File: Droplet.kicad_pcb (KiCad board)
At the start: 2 copper layers, 34.6 x 16.4 mm, 34 parts, among them J1 Conn_01x05, J10 Conn_01x01, J11 Conn_01x01, J12 Conn_01x01, J2 Conn_01x05, J3 Conn_01x01, J4 Conn_01x01, J5 Conn_01x01, J6 Conn_01x01, J7 Conn_01x01, J8 Conn_01x01, J9 Conn_01x01, U1 ATtiny202-SS, U2 IRM-H638T/TR2

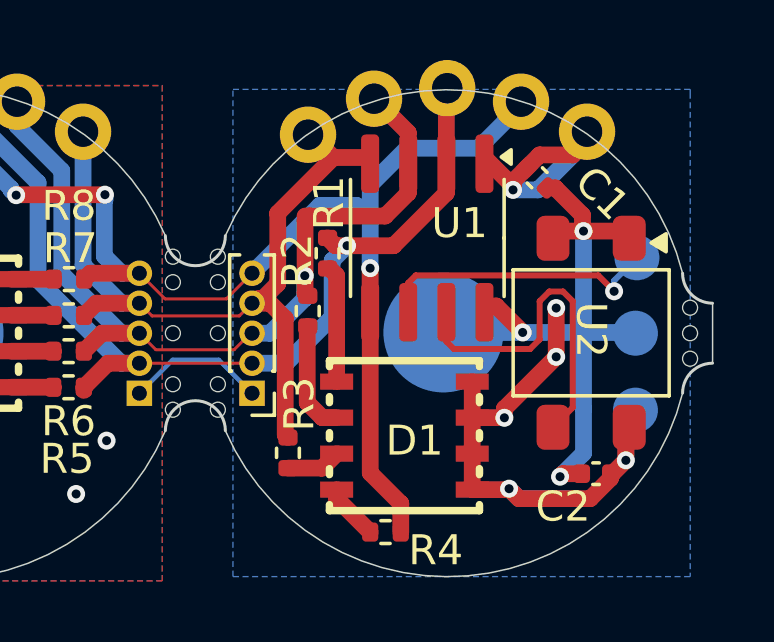
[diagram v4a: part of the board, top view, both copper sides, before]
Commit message: add larger battery terminal
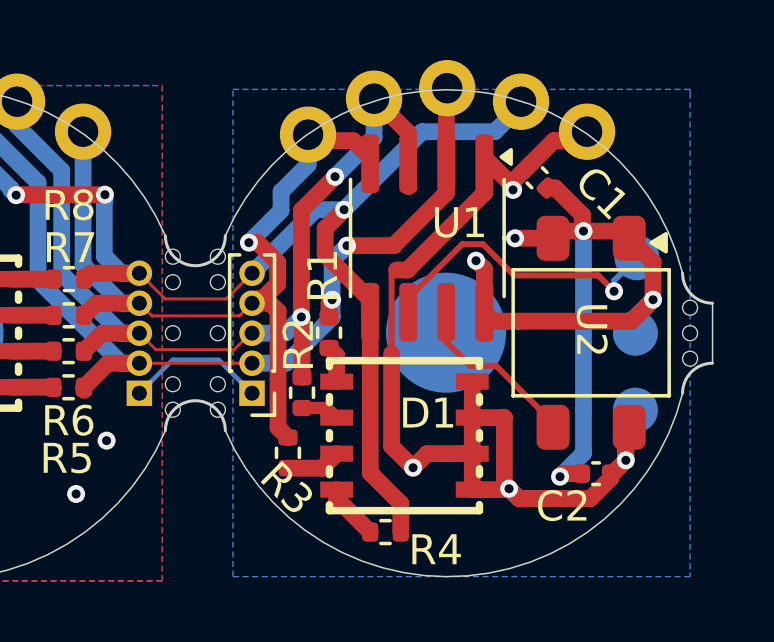
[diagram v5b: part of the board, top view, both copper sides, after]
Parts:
- moved R2 2.73 mm to (113.5, 36.4)
- moved R1 2.65 mm to (114.4, 34.4)
- moved TP2 0.09 mm to (118.3, 34.4)
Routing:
- net VBATT: track 35.1 -> 45.2 mm, vias 16 -> 14
- net GND: track 22.2 -> 28.6 mm, vias 3 -> 5
- net /PA3: track 11.4 -> 5.81 mm
- net Net-(D1-Pad2): track 3.94 -> 1.29 mm
- net Net-(D1-Pad4): track 3.74 -> 1.29 mm
- net /PA7: track 30.6 -> 32.4 mm, vias 1 -> 2
- net /PA1: track 27.5 -> 29.3 mm, vias 0 -> 1
- net /PA0: track 10.6 -> 11.1 mm
- net /PA6: track 33.2 -> 33.1 mm, vias 1 -> 2

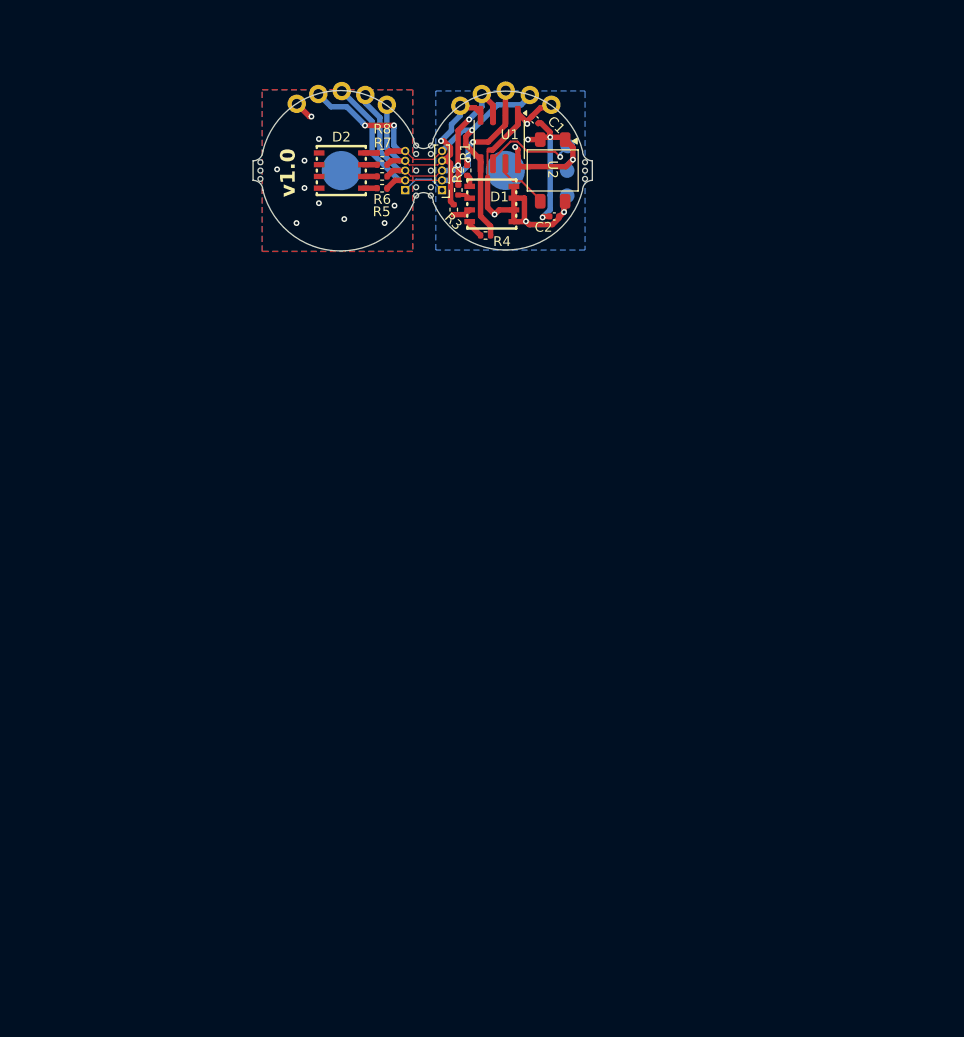
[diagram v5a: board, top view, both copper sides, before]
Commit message: 10 LED pair panel
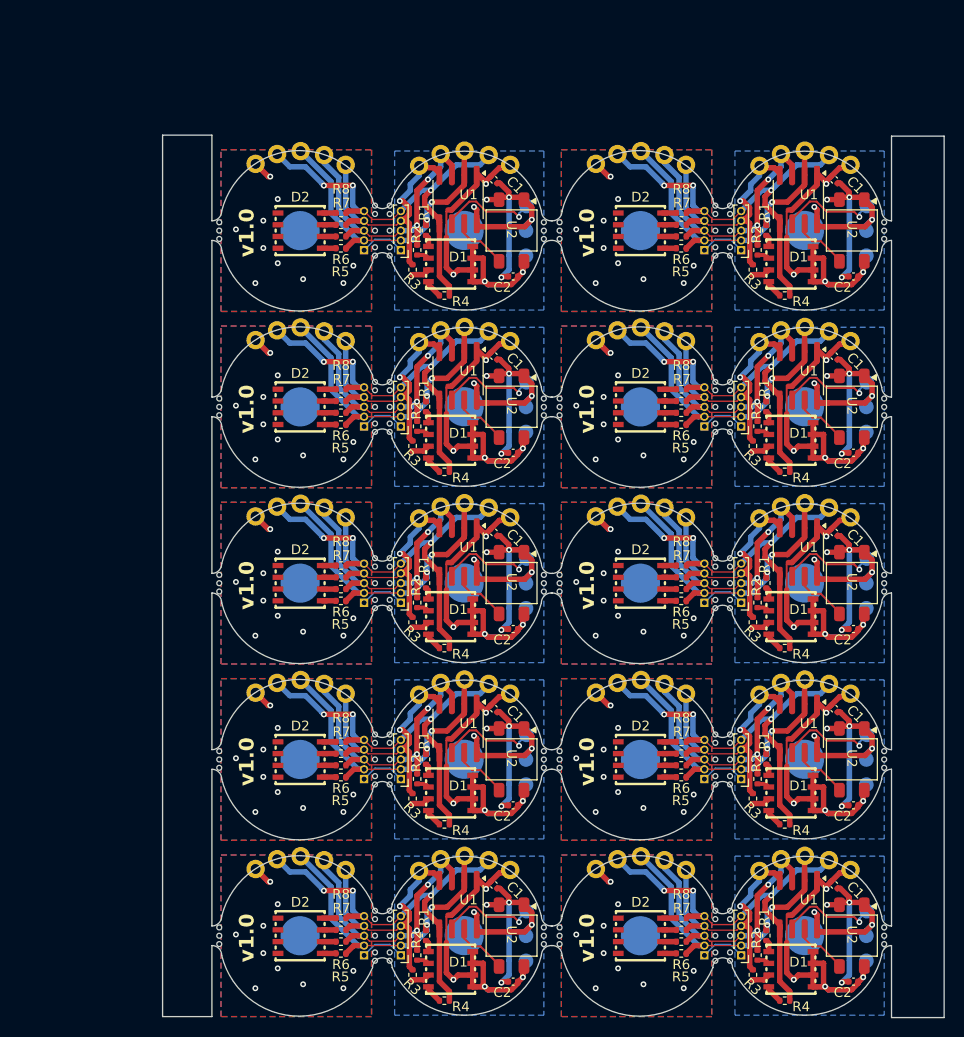
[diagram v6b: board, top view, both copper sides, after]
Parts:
- added C1: 100nF, Capacitor_SMD:C_0402_1005Metric, F.Cu at (117.1, 53.4)
- added C1: 100nF, Capacitor_SMD:C_0402_1005Metric, F.Cu at (151.9, 35.4)
- added C1: 100nF, Capacitor_SMD:C_0402_1005Metric, F.Cu at (151.9, 71.4)
- added C1: 100nF, Capacitor_SMD:C_0402_1005Metric, F.Cu at (117.1, 89.4)
- added C1: 100nF, Capacitor_SMD:C_0402_1005Metric, F.Cu at (151.9, 53.4)
- added C1: 100nF, Capacitor_SMD:C_0402_1005Metric, F.Cu at (117.1, 107.4)
- added C1: 100nF, Capacitor_SMD:C_0402_1005Metric, F.Cu at (117.1, 71.4)
- added C1: 100nF, Capacitor_SMD:C_0402_1005Metric, F.Cu at (117.1, 35.4)
- added C1: 100nF, Capacitor_SMD:C_0402_1005Metric, F.Cu at (151.9, 89.4)
- added C2: 100nF, Capacitor_SMD:C_0402_1005Metric, F.Cu at (119.1, 117.2)
- added C2: 100nF, Capacitor_SMD:C_0402_1005Metric, F.Cu at (119.1, 63.2)
- added C2: 100nF, Capacitor_SMD:C_0402_1005Metric, F.Cu at (119.1, 99.2)
- added C2: 100nF, Capacitor_SMD:C_0402_1005Metric, F.Cu at (153.8, 45.2)
- added C2: 100nF, Capacitor_SMD:C_0402_1005Metric, F.Cu at (153.8, 63.2)
- added C2: 100nF, Capacitor_SMD:C_0402_1005Metric, F.Cu at (119.1, 81.2)
- added C2: 100nF, Capacitor_SMD:C_0402_1005Metric, F.Cu at (153.8, 99.2)
- added C2: 100nF, Capacitor_SMD:C_0402_1005Metric, F.Cu at (153.8, 81.2)
- added C2: 100nF, Capacitor_SMD:C_0402_1005Metric, F.Cu at (119.1, 45.2)
- added D1: HL-5050RGBW-S1-A27, easyeda2kicad:LED-SMD_8P-L5.0-W5.0-P1.20_HL-5050RGBW-S1-A27, F.Cu at (147.5, 80.0)
- added D1: HL-5050RGBW-S1-A27, easyeda2kicad:LED-SMD_8P-L5.0-W5.0-P1.20_HL-5050RGBW-S1-A27, F.Cu at (112.7, 62.0)
- added D1: HL-5050RGBW-S1-A27, easyeda2kicad:LED-SMD_8P-L5.0-W5.0-P1.20_HL-5050RGBW-S1-A27, F.Cu at (112.7, 98.0)
- added D1: HL-5050RGBW-S1-A27, easyeda2kicad:LED-SMD_8P-L5.0-W5.0-P1.20_HL-5050RGBW-S1-A27, F.Cu at (147.5, 62.0)
- added D1: HL-5050RGBW-S1-A27, easyeda2kicad:LED-SMD_8P-L5.0-W5.0-P1.20_HL-5050RGBW-S1-A27, F.Cu at (147.5, 44.0)
- added D1: HL-5050RGBW-S1-A27, easyeda2kicad:LED-SMD_8P-L5.0-W5.0-P1.20_HL-5050RGBW-S1-A27, F.Cu at (112.7, 116.0)
- added D1: HL-5050RGBW-S1-A27, easyeda2kicad:LED-SMD_8P-L5.0-W5.0-P1.20_HL-5050RGBW-S1-A27, F.Cu at (112.7, 44.0)
- added D1: HL-5050RGBW-S1-A27, easyeda2kicad:LED-SMD_8P-L5.0-W5.0-P1.20_HL-5050RGBW-S1-A27, F.Cu at (147.5, 98.0)
- added D1: HL-5050RGBW-S1-A27, easyeda2kicad:LED-SMD_8P-L5.0-W5.0-P1.20_HL-5050RGBW-S1-A27, F.Cu at (112.7, 80.0)
- added D2: HL-5050RGBW-S1-A27, easyeda2kicad:LED-SMD_8P-L5.0-W5.0-P1.20_HL-5050RGBW-S1-A27, F.Cu at (97.3, 40.5)
- added D2: HL-5050RGBW-S1-A27, easyeda2kicad:LED-SMD_8P-L5.0-W5.0-P1.20_HL-5050RGBW-S1-A27, F.Cu at (132.1, 40.5)
- added D2: HL-5050RGBW-S1-A27, easyeda2kicad:LED-SMD_8P-L5.0-W5.0-P1.20_HL-5050RGBW-S1-A27, F.Cu at (132.1, 58.5)
- added D2: HL-5050RGBW-S1-A27, easyeda2kicad:LED-SMD_8P-L5.0-W5.0-P1.20_HL-5050RGBW-S1-A27, F.Cu at (97.3, 94.5)
- added D2: HL-5050RGBW-S1-A27, easyeda2kicad:LED-SMD_8P-L5.0-W5.0-P1.20_HL-5050RGBW-S1-A27, F.Cu at (97.3, 112.5)
- added D2: HL-5050RGBW-S1-A27, easyeda2kicad:LED-SMD_8P-L5.0-W5.0-P1.20_HL-5050RGBW-S1-A27, F.Cu at (97.3, 58.5)
- added D2: HL-5050RGBW-S1-A27, easyeda2kicad:LED-SMD_8P-L5.0-W5.0-P1.20_HL-5050RGBW-S1-A27, F.Cu at (132.1, 94.5)
- added D2: HL-5050RGBW-S1-A27, easyeda2kicad:LED-SMD_8P-L5.0-W5.0-P1.20_HL-5050RGBW-S1-A27, F.Cu at (132.1, 76.5)
- added D2: HL-5050RGBW-S1-A27, easyeda2kicad:LED-SMD_8P-L5.0-W5.0-P1.20_HL-5050RGBW-S1-A27, F.Cu at (97.3, 76.5)
- added J1: Conn_01x05, Connector_PinHeader_1.00mm:PinHeader_1x05_P1.00mm_Vertical, B.Cu at (103.9, 78.5)
- added J1: Conn_01x05, Connector_PinHeader_1.00mm:PinHeader_1x05_P1.00mm_Vertical, B.Cu at (138.6, 78.5)
- added J1: Conn_01x05, Connector_PinHeader_1.00mm:PinHeader_1x05_P1.00mm_Vertical, B.Cu at (103.9, 96.5)
- added J1: Conn_01x05, Connector_PinHeader_1.00mm:PinHeader_1x05_P1.00mm_Vertical, B.Cu at (138.6, 42.5)
- added J1: Conn_01x05, Connector_PinHeader_1.00mm:PinHeader_1x05_P1.00mm_Vertical, B.Cu at (103.9, 60.5)
- added J1: Conn_01x05, Connector_PinHeader_1.00mm:PinHeader_1x05_P1.00mm_Vertical, B.Cu at (138.6, 60.5)
- added J1: Conn_01x05, Connector_PinHeader_1.00mm:PinHeader_1x05_P1.00mm_Vertical, B.Cu at (138.6, 96.5)
- added J1: Conn_01x05, Connector_PinHeader_1.00mm:PinHeader_1x05_P1.00mm_Vertical, B.Cu at (103.9, 114.5)
- added J1: Conn_01x05, Connector_PinHeader_1.00mm:PinHeader_1x05_P1.00mm_Vertical, B.Cu at (103.9, 42.5)
- added J10: Conn_01x01, Custom:1x01_P2.54mm castellated, F.Cu at (134.5, 50.8)
- added J10: Conn_01x01, Custom:1x01_P2.54mm castellated, F.Cu at (99.8, 86.8)
- added J10: Conn_01x01, Custom:1x01_P2.54mm castellated, F.Cu at (99.8, 104.8)
- added J10: Conn_01x01, Custom:1x01_P2.54mm castellated, F.Cu at (134.5, 32.8)
- added J10: Conn_01x01, Custom:1x01_P2.54mm castellated, F.Cu at (134.5, 68.8)
- added J10: Conn_01x01, Custom:1x01_P2.54mm castellated, F.Cu at (99.8, 32.8)
- added J10: Conn_01x01, Custom:1x01_P2.54mm castellated, F.Cu at (99.8, 50.8)
- added J10: Conn_01x01, Custom:1x01_P2.54mm castellated, F.Cu at (99.8, 68.8)
- added J10: Conn_01x01, Custom:1x01_P2.54mm castellated, F.Cu at (134.5, 86.8)
- added J11: Conn_01x01, Custom:1x01_P2.54mm castellated, F.Cu at (97.4, 68.4)
- added J11: Conn_01x01, Custom:1x01_P2.54mm castellated, F.Cu at (97.4, 32.4)
- added J11: Conn_01x01, Custom:1x01_P2.54mm castellated, F.Cu at (97.4, 104.4)
- added J11: Conn_01x01, Custom:1x01_P2.54mm castellated, F.Cu at (132.1, 68.4)
- added J11: Conn_01x01, Custom:1x01_P2.54mm castellated, F.Cu at (97.4, 50.4)
- added J11: Conn_01x01, Custom:1x01_P2.54mm castellated, F.Cu at (97.4, 86.4)
- added J11: Conn_01x01, Custom:1x01_P2.54mm castellated, F.Cu at (132.1, 50.4)
- added J11: Conn_01x01, Custom:1x01_P2.54mm castellated, F.Cu at (132.1, 86.4)
- added J11: Conn_01x01, Custom:1x01_P2.54mm castellated, F.Cu at (132.1, 32.4)
- added J12: Conn_01x01, Custom:1x01_P2.54mm castellated, F.Cu at (92.8, 105.7)
- added J12: Conn_01x01, Custom:1x01_P2.54mm castellated, F.Cu at (92.8, 51.7)
- added J12: Conn_01x01, Custom:1x01_P2.54mm castellated, F.Cu at (92.8, 87.7)
- added J12: Conn_01x01, Custom:1x01_P2.54mm castellated, F.Cu at (127.5, 51.7)
- added J12: Conn_01x01, Custom:1x01_P2.54mm castellated, F.Cu at (127.5, 87.7)
- added J12: Conn_01x01, Custom:1x01_P2.54mm castellated, F.Cu at (92.8, 69.7)
- added J12: Conn_01x01, Custom:1x01_P2.54mm castellated, F.Cu at (127.5, 69.7)
- added J12: Conn_01x01, Custom:1x01_P2.54mm castellated, F.Cu at (92.8, 33.7)
- added J12: Conn_01x01, Custom:1x01_P2.54mm castellated, F.Cu at (127.5, 33.7)
- added J2: Conn_01x05, Connector_PinHeader_1.00mm:PinHeader_1x05_P1.00mm_Vertical, F.Cu at (142.4, 78.5)
- added J2: Conn_01x05, Connector_PinHeader_1.00mm:PinHeader_1x05_P1.00mm_Vertical, F.Cu at (107.6, 42.5)
- added J2: Conn_01x05, Connector_PinHeader_1.00mm:PinHeader_1x05_P1.00mm_Vertical, F.Cu at (107.6, 78.5)
- added J2: Conn_01x05, Connector_PinHeader_1.00mm:PinHeader_1x05_P1.00mm_Vertical, F.Cu at (142.4, 60.5)
- added J2: Conn_01x05, Connector_PinHeader_1.00mm:PinHeader_1x05_P1.00mm_Vertical, F.Cu at (107.6, 96.5)
- added J2: Conn_01x05, Connector_PinHeader_1.00mm:PinHeader_1x05_P1.00mm_Vertical, F.Cu at (142.4, 42.5)
- added J2: Conn_01x05, Connector_PinHeader_1.00mm:PinHeader_1x05_P1.00mm_Vertical, F.Cu at (142.4, 96.5)
- added J2: Conn_01x05, Connector_PinHeader_1.00mm:PinHeader_1x05_P1.00mm_Vertical, F.Cu at (107.6, 60.5)
- added J2: Conn_01x05, Connector_PinHeader_1.00mm:PinHeader_1x05_P1.00mm_Vertical, F.Cu at (107.6, 114.5)
- added J3: Conn_01x01, Custom:1x01_P2.54mm castellated, F.Cu at (114.1, 86.4)
- added J3: Conn_01x01, Custom:1x01_P2.54mm castellated, F.Cu at (114.1, 68.4)
- added J3: Conn_01x01, Custom:1x01_P2.54mm castellated, F.Cu at (148.9, 86.4)
- added J3: Conn_01x01, Custom:1x01_P2.54mm castellated, F.Cu at (148.9, 32.4)
- added J3: Conn_01x01, Custom:1x01_P2.54mm castellated, F.Cu at (114.1, 50.4)
- added J3: Conn_01x01, Custom:1x01_P2.54mm castellated, F.Cu at (114.1, 32.4)
- added J3: Conn_01x01, Custom:1x01_P2.54mm castellated, F.Cu at (148.9, 50.4)
- added J3: Conn_01x01, Custom:1x01_P2.54mm castellated, F.Cu at (148.9, 68.4)
- added J3: Conn_01x01, Custom:1x01_P2.54mm castellated, F.Cu at (114.1, 104.4)
- added J4: Conn_01x01, Custom:1x01_P2.54mm castellated, F.Cu at (146.4, 50.7)
- added J4: Conn_01x01, Custom:1x01_P2.54mm castellated, F.Cu at (111.7, 86.7)
- added J4: Conn_01x01, Custom:1x01_P2.54mm castellated, F.Cu at (111.7, 50.7)
- added J4: Conn_01x01, Custom:1x01_P2.54mm castellated, F.Cu at (111.7, 68.7)
- added J4: Conn_01x01, Custom:1x01_P2.54mm castellated, F.Cu at (146.4, 68.7)
- added J4: Conn_01x01, Custom:1x01_P2.54mm castellated, F.Cu at (146.4, 86.7)
- added J4: Conn_01x01, Custom:1x01_P2.54mm castellated, F.Cu at (111.7, 104.7)
- added J4: Conn_01x01, Custom:1x01_P2.54mm castellated, F.Cu at (146.4, 32.7)
- added J4: Conn_01x01, Custom:1x01_P2.54mm castellated, F.Cu at (111.7, 32.7)
- added J5: Conn_01x01, Custom:1x01_P2.54mm castellated, F.Cu at (109.5, 87.9)
- added J5: Conn_01x01, Custom:1x01_P2.54mm castellated, F.Cu at (109.5, 33.9)
- added J5: Conn_01x01, Custom:1x01_P2.54mm castellated, F.Cu at (144.2, 51.9)
- added J5: Conn_01x01, Custom:1x01_P2.54mm castellated, F.Cu at (109.5, 105.9)
- added J5: Conn_01x01, Custom:1x01_P2.54mm castellated, F.Cu at (144.2, 69.9)
- added J5: Conn_01x01, Custom:1x01_P2.54mm castellated, F.Cu at (144.2, 87.9)
- added J5: Conn_01x01, Custom:1x01_P2.54mm castellated, F.Cu at (109.5, 51.9)
- added J5: Conn_01x01, Custom:1x01_P2.54mm castellated, F.Cu at (109.5, 69.9)
- added J5: Conn_01x01, Custom:1x01_P2.54mm castellated, F.Cu at (144.2, 33.9)
- added J6: Conn_01x01, Custom:1x01_P2.54mm castellated, F.Cu at (116.6, 32.8)
- added J6: Conn_01x01, Custom:1x01_P2.54mm castellated, F.Cu at (151.3, 32.8)
- added J6: Conn_01x01, Custom:1x01_P2.54mm castellated, F.Cu at (151.3, 86.8)
- added J6: Conn_01x01, Custom:1x01_P2.54mm castellated, F.Cu at (116.6, 68.8)
- added J6: Conn_01x01, Custom:1x01_P2.54mm castellated, F.Cu at (116.6, 86.8)
- added J6: Conn_01x01, Custom:1x01_P2.54mm castellated, F.Cu at (151.3, 50.8)
- added J6: Conn_01x01, Custom:1x01_P2.54mm castellated, F.Cu at (151.3, 68.8)
- added J6: Conn_01x01, Custom:1x01_P2.54mm castellated, F.Cu at (116.6, 50.8)
- added J6: Conn_01x01, Custom:1x01_P2.54mm castellated, F.Cu at (116.6, 104.8)
- added J7: Conn_01x01, Custom:1x01_P2.54mm castellated, F.Cu at (153.5, 33.8)
- added J7: Conn_01x01, Custom:1x01_P2.54mm castellated, F.Cu at (118.8, 87.8)
- added J7: Conn_01x01, Custom:1x01_P2.54mm castellated, F.Cu at (118.8, 51.8)
- added J7: Conn_01x01, Custom:1x01_P2.54mm castellated, F.Cu at (153.5, 69.8)
- added J7: Conn_01x01, Custom:1x01_P2.54mm castellated, F.Cu at (118.8, 105.8)
- added J7: Conn_01x01, Custom:1x01_P2.54mm castellated, F.Cu at (118.8, 33.8)
- added J7: Conn_01x01, Custom:1x01_P2.54mm castellated, F.Cu at (153.5, 51.8)
- added J7: Conn_01x01, Custom:1x01_P2.54mm castellated, F.Cu at (118.8, 69.8)
- added J7: Conn_01x01, Custom:1x01_P2.54mm castellated, F.Cu at (153.5, 87.8)
- added J8: Conn_01x01, Custom:1x01_P2.54mm castellated, F.Cu at (95.0, 86.7)
- added J8: Conn_01x01, Custom:1x01_P2.54mm castellated, F.Cu at (129.7, 86.7)
- added J8: Conn_01x01, Custom:1x01_P2.54mm castellated, F.Cu at (129.7, 50.7)
- added J8: Conn_01x01, Custom:1x01_P2.54mm castellated, F.Cu at (129.7, 68.7)
- added J8: Conn_01x01, Custom:1x01_P2.54mm castellated, F.Cu at (95.0, 50.7)
- added J8: Conn_01x01, Custom:1x01_P2.54mm castellated, F.Cu at (95.0, 104.7)
- added J8: Conn_01x01, Custom:1x01_P2.54mm castellated, F.Cu at (95.0, 32.7)
- added J8: Conn_01x01, Custom:1x01_P2.54mm castellated, F.Cu at (95.0, 68.7)
- added J8: Conn_01x01, Custom:1x01_P2.54mm castellated, F.Cu at (129.7, 32.7)
- added J9: Conn_01x01, Custom:1x01_P2.54mm castellated, F.Cu at (102.0, 105.8)
- added J9: Conn_01x01, Custom:1x01_P2.54mm castellated, F.Cu at (136.7, 87.8)
- added J9: Conn_01x01, Custom:1x01_P2.54mm castellated, F.Cu at (102.0, 69.8)
- added J9: Conn_01x01, Custom:1x01_P2.54mm castellated, F.Cu at (136.7, 51.8)
- added J9: Conn_01x01, Custom:1x01_P2.54mm castellated, F.Cu at (102.0, 87.8)
- added J9: Conn_01x01, Custom:1x01_P2.54mm castellated, F.Cu at (136.7, 33.8)
- added J9: Conn_01x01, Custom:1x01_P2.54mm castellated, F.Cu at (102.0, 51.8)
- added J9: Conn_01x01, Custom:1x01_P2.54mm castellated, F.Cu at (136.7, 69.8)
- added J9: Conn_01x01, Custom:1x01_P2.54mm castellated, F.Cu at (102.0, 33.8)
- added R1: 27, Resistor_SMD:R_0402_1005Metric, F.Cu at (110.2, 58.5)
- added R1: 27, Resistor_SMD:R_0402_1005Metric, F.Cu at (144.9, 76.5)
- added R1: 27, Resistor_SMD:R_0402_1005Metric, F.Cu at (110.2, 40.5)
- added R1: 27, Resistor_SMD:R_0402_1005Metric, F.Cu at (144.9, 94.5)
- added R1: 27, Resistor_SMD:R_0402_1005Metric, F.Cu at (110.2, 94.5)
- added R1: 27, Resistor_SMD:R_0402_1005Metric, F.Cu at (110.2, 112.5)
- added R1: 27, Resistor_SMD:R_0402_1005Metric, F.Cu at (144.9, 58.5)
- added R1: 27, Resistor_SMD:R_0402_1005Metric, F.Cu at (110.2, 76.5)
- added R1: 27, Resistor_SMD:R_0402_1005Metric, F.Cu at (144.9, 40.5)
- added R2: 27, Resistor_SMD:R_0402_1005Metric, F.Cu at (144.0, 78.5)
- added R2: 27, Resistor_SMD:R_0402_1005Metric, F.Cu at (109.3, 60.5)
- added R2: 27, Resistor_SMD:R_0402_1005Metric, F.Cu at (109.3, 96.5)
- added R2: 27, Resistor_SMD:R_0402_1005Metric, F.Cu at (109.3, 114.5)
- added R2: 27, Resistor_SMD:R_0402_1005Metric, F.Cu at (144.0, 96.5)
- added R2: 27, Resistor_SMD:R_0402_1005Metric, F.Cu at (144.0, 60.5)
- added R2: 27, Resistor_SMD:R_0402_1005Metric, F.Cu at (109.3, 78.5)
- added R2: 27, Resistor_SMD:R_0402_1005Metric, F.Cu at (144.0, 42.5)
- added R2: 27, Resistor_SMD:R_0402_1005Metric, F.Cu at (109.3, 42.5)
- added R3: 27, Resistor_SMD:R_0402_1005Metric, F.Cu at (108.8, 62.5)
- added R3: 27, Resistor_SMD:R_0402_1005Metric, F.Cu at (143.6, 44.5)
- added R3: 27, Resistor_SMD:R_0402_1005Metric, F.Cu at (108.8, 98.5)
- added R3: 27, Resistor_SMD:R_0402_1005Metric, F.Cu at (143.6, 62.5)
- added R3: 27, Resistor_SMD:R_0402_1005Metric, F.Cu at (108.8, 116.5)
- added R3: 27, Resistor_SMD:R_0402_1005Metric, F.Cu at (143.6, 98.5)
- added R3: 27, Resistor_SMD:R_0402_1005Metric, F.Cu at (143.6, 80.5)
- added R3: 27, Resistor_SMD:R_0402_1005Metric, F.Cu at (108.8, 80.5)
- added R3: 27, Resistor_SMD:R_0402_1005Metric, F.Cu at (108.8, 44.5)
- added R4: 75, Resistor_SMD:R_0402_1005Metric, F.Cu at (146.8, 101.2)
- added R4: 75, Resistor_SMD:R_0402_1005Metric, F.Cu at (112.1, 83.2)
- added R4: 75, Resistor_SMD:R_0402_1005Metric, F.Cu at (146.8, 83.2)
- added R4: 75, Resistor_SMD:R_0402_1005Metric, F.Cu at (112.1, 65.2)
- added R4: 75, Resistor_SMD:R_0402_1005Metric, F.Cu at (112.1, 47.2)
- added R4: 75, Resistor_SMD:R_0402_1005Metric, F.Cu at (112.1, 119.2)
- added R4: 75, Resistor_SMD:R_0402_1005Metric, F.Cu at (112.1, 101.2)
- added R4: 75, Resistor_SMD:R_0402_1005Metric, F.Cu at (146.8, 65.2)
- added R4: 75, Resistor_SMD:R_0402_1005Metric, F.Cu at (146.8, 47.2)
- added R5: 27, Resistor_SMD:R_0402_1005Metric, F.Cu at (101.5, 78.4)
- added R5: 27, Resistor_SMD:R_0402_1005Metric, F.Cu at (101.5, 60.4)
- added R5: 27, Resistor_SMD:R_0402_1005Metric, F.Cu at (136.3, 78.4)
- added R5: 27, Resistor_SMD:R_0402_1005Metric, F.Cu at (101.5, 96.4)
- added R5: 27, Resistor_SMD:R_0402_1005Metric, F.Cu at (136.3, 60.4)
- added R5: 27, Resistor_SMD:R_0402_1005Metric, F.Cu at (136.3, 42.4)
- added R5: 27, Resistor_SMD:R_0402_1005Metric, F.Cu at (101.5, 42.4)
- added R5: 27, Resistor_SMD:R_0402_1005Metric, F.Cu at (101.5, 114.4)
- added R5: 27, Resistor_SMD:R_0402_1005Metric, F.Cu at (136.3, 96.4)
- added R6: 27, Resistor_SMD:R_0402_1005Metric, F.Cu at (136.3, 77.1)
- added R6: 27, Resistor_SMD:R_0402_1005Metric, F.Cu at (136.3, 95.1)
- added R6: 27, Resistor_SMD:R_0402_1005Metric, F.Cu at (101.5, 113.1)
- added R6: 27, Resistor_SMD:R_0402_1005Metric, F.Cu at (101.5, 59.1)
- added R6: 27, Resistor_SMD:R_0402_1005Metric, F.Cu at (101.5, 41.1)
- added R6: 27, Resistor_SMD:R_0402_1005Metric, F.Cu at (136.3, 59.1)
- added R6: 27, Resistor_SMD:R_0402_1005Metric, F.Cu at (101.5, 77.1)
- added R6: 27, Resistor_SMD:R_0402_1005Metric, F.Cu at (101.5, 95.1)
- added R6: 27, Resistor_SMD:R_0402_1005Metric, F.Cu at (136.3, 41.1)
- added R7: 27, Resistor_SMD:R_0402_1005Metric, F.Cu at (136.3, 40.0)
- added R7: 27, Resistor_SMD:R_0402_1005Metric, F.Cu at (101.5, 112.0)
- added R7: 27, Resistor_SMD:R_0402_1005Metric, F.Cu at (101.5, 76.0)
- added R7: 27, Resistor_SMD:R_0402_1005Metric, F.Cu at (101.5, 94.0)
- added R7: 27, Resistor_SMD:R_0402_1005Metric, F.Cu at (101.5, 40.0)
- added R7: 27, Resistor_SMD:R_0402_1005Metric, F.Cu at (136.3, 94.0)
- added R7: 27, Resistor_SMD:R_0402_1005Metric, F.Cu at (136.3, 76.0)
- added R7: 27, Resistor_SMD:R_0402_1005Metric, F.Cu at (101.5, 58.0)
- added R7: 27, Resistor_SMD:R_0402_1005Metric, F.Cu at (136.3, 58.0)
- added R8: 75, Resistor_SMD:R_0402_1005Metric, F.Cu at (101.5, 74.7)
- added R8: 75, Resistor_SMD:R_0402_1005Metric, F.Cu at (101.5, 56.7)
- added R8: 75, Resistor_SMD:R_0402_1005Metric, F.Cu at (136.3, 38.7)
- added R8: 75, Resistor_SMD:R_0402_1005Metric, F.Cu at (101.5, 38.7)
- added R8: 75, Resistor_SMD:R_0402_1005Metric, F.Cu at (136.3, 92.7)
- added R8: 75, Resistor_SMD:R_0402_1005Metric, F.Cu at (136.3, 74.7)
- added R8: 75, Resistor_SMD:R_0402_1005Metric, F.Cu at (101.5, 92.7)
- added R8: 75, Resistor_SMD:R_0402_1005Metric, F.Cu at (136.3, 56.7)
- added R8: 75, Resistor_SMD:R_0402_1005Metric, F.Cu at (101.5, 110.7)
- added REF**: MouseBite-Slot_2.0x4.5mm_outset_D0.5mm_P0.85mm_5h_Trace, Panelization:MouseBite-Slot_2.0x4.5mm_outset_D0.5mm_P0.85mm_5h_Trace, F.Cu at (106.7, 76.5)
- added REF**: MouseBite-Part_2.0x2.0mm_outset_D0.5mm_P0.85mm_3h, Panelization:MouseBite-Part_2.0x2.0mm_outset_D0.5mm_P0.85mm_3h, F.Cu at (124.1, 58.5)
- added REF**: MouseBite-Slot_2.0x4.5mm_outset_D0.5mm_P0.85mm_5h_Trace, Panelization:MouseBite-Slot_2.0x4.5mm_outset_D0.5mm_P0.85mm_5h_Trace, F.Cu at (141.5, 58.5)
- added REF**: MouseBite-Slot_2.0x4.5mm_outset_D0.5mm_P0.85mm_5h_Trace, Panelization:MouseBite-Slot_2.0x4.5mm_outset_D0.5mm_P0.85mm_5h_Trace, F.Cu at (141.5, 76.5)
- added REF**: MouseBite-Part_2.0x2.0mm_outset_D0.5mm_P0.85mm_3h, Panelization:MouseBite-Part_2.0x2.0mm_outset_D0.5mm_P0.85mm_3h, F.Cu at (156.7, 94.5)
- added REF**: MouseBite-Part_2.0x2.0mm_outset_D0.5mm_P0.85mm_3h, Panelization:MouseBite-Part_2.0x2.0mm_outset_D0.5mm_P0.85mm_3h, F.Cu at (122.0, 58.5)
- added REF**: MouseBite-Part_2.0x2.0mm_outset_D0.5mm_P0.85mm_3h, Panelization:MouseBite-Part_2.0x2.0mm_outset_D0.5mm_P0.85mm_3h, F.Cu at (122.0, 40.5)
- added REF**: MouseBite-Part_2.0x2.0mm_outset_D0.5mm_P0.85mm_3h, Panelization:MouseBite-Part_2.0x2.0mm_outset_D0.5mm_P0.85mm_3h, F.Cu at (89.3, 58.5)
- added REF**: MouseBite-Part_2.0x2.0mm_outset_D0.5mm_P0.85mm_3h, Panelization:MouseBite-Part_2.0x2.0mm_outset_D0.5mm_P0.85mm_3h, F.Cu at (89.3, 94.5)
- added REF**: MouseBite-Part_2.0x2.0mm_outset_D0.5mm_P0.85mm_3h, Panelization:MouseBite-Part_2.0x2.0mm_outset_D0.5mm_P0.85mm_3h, F.Cu at (124.1, 76.5)
- added REF**: MouseBite-Part_2.0x2.0mm_outset_D0.5mm_P0.85mm_3h, Panelization:MouseBite-Part_2.0x2.0mm_outset_D0.5mm_P0.85mm_3h, F.Cu at (124.1, 40.5)
- added REF**: MouseBite-Part_2.0x2.0mm_outset_D0.5mm_P0.85mm_3h, Panelization:MouseBite-Part_2.0x2.0mm_outset_D0.5mm_P0.85mm_3h, F.Cu at (89.3, 40.5)
- added REF**: MouseBite-Part_2.0x2.0mm_outset_D0.5mm_P0.85mm_3h, Panelization:MouseBite-Part_2.0x2.0mm_outset_D0.5mm_P0.85mm_3h, F.Cu at (156.7, 76.5)
- added REF**: MouseBite-Part_2.0x2.0mm_outset_D0.5mm_P0.85mm_3h, Panelization:MouseBite-Part_2.0x2.0mm_outset_D0.5mm_P0.85mm_3h, F.Cu at (124.1, 94.5)
- added REF**: MouseBite-Part_2.0x2.0mm_outset_D0.5mm_P0.85mm_3h, Panelization:MouseBite-Part_2.0x2.0mm_outset_D0.5mm_P0.85mm_3h, F.Cu at (122.0, 76.5)
- added REF**: MouseBite-Slot_2.0x4.5mm_outset_D0.5mm_P0.85mm_5h_Trace, Panelization:MouseBite-Slot_2.0x4.5mm_outset_D0.5mm_P0.85mm_5h_Trace, F.Cu at (106.7, 94.5)
- added REF**: MouseBite-Slot_2.0x4.5mm_outset_D0.5mm_P0.85mm_5h_Trace, Panelization:MouseBite-Slot_2.0x4.5mm_outset_D0.5mm_P0.85mm_5h_Trace, F.Cu at (141.5, 40.5)
- added REF**: MouseBite-Part_2.0x2.0mm_outset_D0.5mm_P0.85mm_3h, Panelization:MouseBite-Part_2.0x2.0mm_outset_D0.5mm_P0.85mm_3h, F.Cu at (122.0, 112.5)
- added REF**: MouseBite-Slot_2.0x4.5mm_outset_D0.5mm_P0.85mm_5h_Trace, Panelization:MouseBite-Slot_2.0x4.5mm_outset_D0.5mm_P0.85mm_5h_Trace, F.Cu at (141.5, 94.5)
- added REF**: MouseBite-Part_2.0x2.0mm_outset_D0.5mm_P0.85mm_3h, Panelization:MouseBite-Part_2.0x2.0mm_outset_D0.5mm_P0.85mm_3h, F.Cu at (122.0, 94.5)
- added REF**: MouseBite-Part_2.0x2.0mm_outset_D0.5mm_P0.85mm_3h, Panelization:MouseBite-Part_2.0x2.0mm_outset_D0.5mm_P0.85mm_3h, F.Cu at (89.3, 112.5)
- added REF**: MouseBite-Slot_2.0x4.5mm_outset_D0.5mm_P0.85mm_5h_Trace, Panelization:MouseBite-Slot_2.0x4.5mm_outset_D0.5mm_P0.85mm_5h_Trace, F.Cu at (106.7, 58.5)
- added REF**: MouseBite-Slot_2.0x4.5mm_outset_D0.5mm_P0.85mm_5h_Trace, Panelization:MouseBite-Slot_2.0x4.5mm_outset_D0.5mm_P0.85mm_5h_Trace, F.Cu at (106.7, 112.5)
- added REF**: MouseBite-Slot_2.0x4.5mm_outset_D0.5mm_P0.85mm_5h_Trace, Panelization:MouseBite-Slot_2.0x4.5mm_outset_D0.5mm_P0.85mm_5h_Trace, F.Cu at (106.7, 40.5)
- added REF**: MouseBite-Part_2.0x2.0mm_outset_D0.5mm_P0.85mm_3h, Panelization:MouseBite-Part_2.0x2.0mm_outset_D0.5mm_P0.85mm_3h, F.Cu at (156.7, 40.5)
- added REF**: MouseBite-Part_2.0x2.0mm_outset_D0.5mm_P0.85mm_3h, Panelization:MouseBite-Part_2.0x2.0mm_outset_D0.5mm_P0.85mm_3h, F.Cu at (89.3, 76.5)
- added REF**: MouseBite-Part_2.0x2.0mm_outset_D0.5mm_P0.85mm_3h, Panelization:MouseBite-Part_2.0x2.0mm_outset_D0.5mm_P0.85mm_3h, F.Cu at (156.7, 58.5)
- added TP1: +, TestPoint:TestPoint_Pad_D4.0mm, B.Cu at (97.3, 112.5)
- added TP1: +, TestPoint:TestPoint_Pad_D4.0mm, B.Cu at (97.3, 58.5)
- added TP1: +, TestPoint:TestPoint_Pad_D4.0mm, B.Cu at (97.3, 94.5)
- added TP1: +, TestPoint:TestPoint_Pad_D4.0mm, B.Cu at (132.1, 40.5)
- added TP1: +, TestPoint:TestPoint_Pad_D4.0mm, B.Cu at (97.3, 76.5)
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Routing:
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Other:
- board size 34.6 x 16.4 mm -> 79.8 x 90.1 mm
- board text added: "CNC"

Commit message: major changes - add boost and mosfets
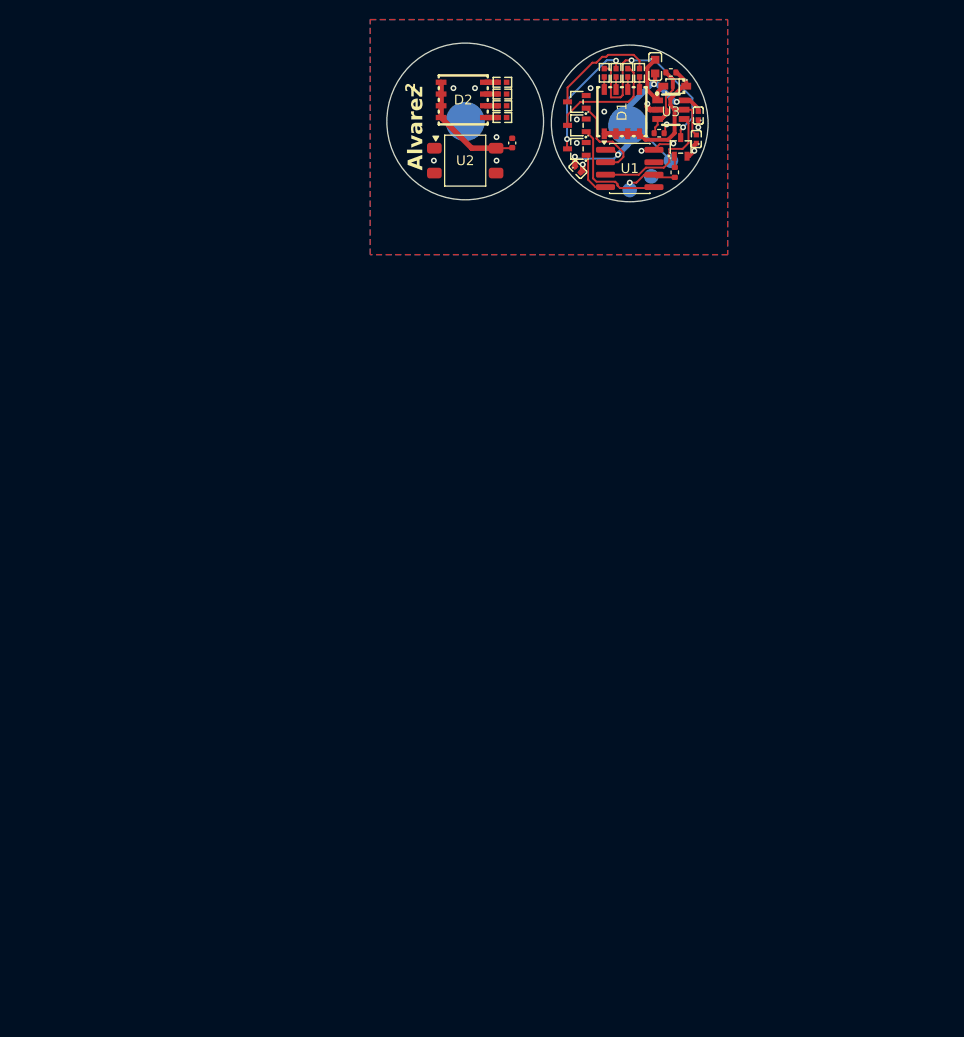
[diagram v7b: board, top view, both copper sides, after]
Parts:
- removed C1 (x10): 100nF, Capacitor_SMD:C_0402_1005Metric
- removed the C2 at (119.1, 117.2)
- removed the C2 at (153.8, 117.2)
- removed the C2 at (119.1, 63.2)
- removed the C2 at (119.1, 99.2)
- removed the C2 at (153.8, 45.2)
- removed the C2 at (153.8, 63.2)
- removed the C2 at (119.1, 81.2)
- removed the C2 at (153.8, 99.2)
- removed the C2 at (153.8, 81.2)
- removed the C2 at (119.1, 45.2)
- removed the D1 at (147.5, 80.0)
- removed the D1 at (112.7, 62.0)
- removed the D1 at (112.7, 98.0)
- removed the D1 at (147.5, 62.0)
- removed the D1 at (147.5, 44.0)
- removed the D1 at (147.5, 116.0)
- removed the D1 at (112.7, 116.0)
- removed the D1 at (112.7, 44.0)
- removed the D1 at (147.5, 98.0)
- removed the D1 at (112.7, 80.0)
- removed the D2 at (97.3, 40.5)
- removed the D2 at (132.1, 112.5)
- removed the D2 at (132.1, 40.5)
- removed the D2 at (132.1, 58.5)
- removed the D2 at (97.3, 94.5)
- removed the D2 at (97.3, 112.5)
- removed the D2 at (97.3, 58.5)
- removed the D2 at (132.1, 94.5)
- removed the D2 at (132.1, 76.5)
- removed the D2 at (97.3, 76.5)
- removed J1 (x10), J2 (x10): Conn_01x05, Connector_PinHeader_1.00mm:PinHeader_1x05_P1.00mm_Vertical
- removed J10 (x10), J11 (x10), J12 (x10), J3 (x10), J4 (x10), J5 (x10), J6 (x10), J7 (x10), J8 (x10), J9 (x10): Conn_01x01, Custom:1x01_P2.54mm castellated
- removed the R1 at (110.2, 58.5)
- removed the R1 at (144.9, 76.5)
- removed the R1 at (110.2, 40.5)
- removed the R1 at (144.9, 94.5)
- removed the R1 at (110.2, 94.5)
- removed the R1 at (110.2, 112.5)
- removed the R1 at (144.9, 58.5)
- removed the R1 at (110.2, 76.5)
- removed the R1 at (144.9, 40.5)
- removed the R1 at (144.9, 112.5)
- removed the R2 at (144.0, 78.5)
- removed the R2 at (109.3, 60.5)
- removed the R2 at (109.3, 96.5)
- removed the R2 at (109.3, 114.5)
- removed the R2 at (144.0, 96.5)
- removed the R2 at (144.0, 60.5)
- removed the R2 at (109.3, 78.5)
- removed the R2 at (144.0, 114.5)
- removed the R2 at (144.0, 42.5)
- removed the R2 at (109.3, 42.5)
- removed the R3 at (108.8, 62.5)
- removed the R3 at (143.6, 44.5)
- removed the R3 at (108.8, 98.5)
- removed the R3 at (143.6, 62.5)
- removed the R3 at (108.8, 116.5)
- removed the R3 at (143.6, 98.5)
- removed the R3 at (143.6, 80.5)
- removed the R3 at (108.8, 80.5)
- removed the R3 at (143.6, 116.5)
- removed the R3 at (108.8, 44.5)
- removed the R4 at (146.8, 101.2)
- removed the R4 at (146.8, 119.2)
- removed the R4 at (112.1, 83.2)
- removed the R4 at (146.8, 83.2)
- removed the R4 at (112.1, 65.2)
- removed the R4 at (112.1, 47.2)
- removed the R4 at (112.1, 119.2)
- removed the R4 at (112.1, 101.2)
- removed the R4 at (146.8, 65.2)
- removed the R4 at (146.8, 47.2)
- removed the R5 at (101.5, 78.4)
- removed the R5 at (101.5, 60.4)
- removed the R5 at (136.3, 78.4)
- removed the R5 at (101.5, 96.4)
- removed the R5 at (136.3, 60.4)
- removed the R5 at (136.3, 42.4)
- removed the R5 at (136.3, 114.4)
- removed the R5 at (101.5, 42.4)
- removed the R5 at (101.5, 114.4)
- removed the R5 at (136.3, 96.4)
- removed the R6 at (136.3, 77.1)
- removed the R6 at (136.3, 95.1)
- removed the R6 at (101.5, 113.1)
- removed the R6 at (101.5, 59.1)
- removed the R6 at (101.5, 41.1)
- removed the R6 at (136.3, 59.1)
- removed the R6 at (136.3, 113.1)
- removed the R6 at (101.5, 77.1)
- removed the R6 at (101.5, 95.1)
- removed the R6 at (136.3, 41.1)
- removed the R7 at (136.3, 40.0)
- removed the R7 at (101.5, 112.0)
- removed the R7 at (136.3, 112.0)
- removed the R7 at (101.5, 76.0)
- removed the R7 at (101.5, 94.0)
- removed the R7 at (101.5, 40.0)
- removed the R7 at (136.3, 94.0)
- removed the R7 at (136.3, 76.0)
- removed the R7 at (101.5, 58.0)
- removed the R7 at (136.3, 58.0)
- removed the R8 at (101.5, 74.7)
- removed the R8 at (101.5, 56.7)
- removed the R8 at (136.3, 38.7)
- removed the R8 at (101.5, 38.7)
- removed the R8 at (136.3, 92.7)
- removed the R8 at (136.3, 74.7)
- removed the R8 at (101.5, 92.7)
- removed the R8 at (136.3, 110.7)
- removed the R8 at (136.3, 56.7)
- removed the R8 at (101.5, 110.7)
- removed REF** (x10): MouseBite-Slot_2.0x4.5mm_outset_D0.5mm_P0.85mm_5h_Trace, Panelization:MouseBite-Slot_2.0x4.5mm_outset_D0.5mm_P0.85mm_5h_Trace
- removed REF** (x20): MouseBite-Part_2.0x2.0mm_outset_D0.5mm_P0.85mm_3h, Panelization:MouseBite-Part_2.0x2.0mm_outset_D0.5mm_P0.85mm_3h
- removed the TP1 at (97.3, 112.5)
- removed the TP1 at (97.3, 58.5)
- removed the TP1 at (132.1, 112.5)
- removed the TP1 at (97.3, 94.5)
- removed the TP1 at (132.1, 40.5)
- removed the TP1 at (97.3, 76.5)
- removed the TP1 at (132.1, 76.5)
- removed the TP1 at (132.1, 58.5)
- removed the TP1 at (97.3, 40.5)
- removed the TP1 at (132.1, 94.5)
- removed the TP2 at (114.1, 94.5)
- removed the TP2 at (148.8, 40.5)
- removed the TP2 at (148.8, 94.5)
- removed the TP2 at (114.1, 58.5)
- removed the TP2 at (114.1, 76.5)
- removed the TP2 at (114.1, 40.5)
- removed the TP2 at (148.8, 58.5)
- removed the TP2 at (148.8, 112.5)
- removed the TP2 at (114.1, 112.5)
- removed the TP2 at (148.8, 76.5)
- removed the TP3 at (120.5, 74.0)
- removed the TP3 at (120.5, 110.0)
- removed the TP3 at (120.5, 56.0)
- removed the TP3 at (155.2, 38.0)
- removed the TP3 at (155.2, 74.0)
- removed the TP3 at (155.2, 92.0)
- removed the TP3 at (155.2, 110.0)
- removed the TP3 at (155.2, 56.0)
- removed the TP3 at (120.5, 92.0)
- removed the TP3 at (120.5, 38.0)
- removed the TP4 at (120.4, 94.5)
- removed the TP4 at (155.2, 94.5)
- removed the TP4 at (120.4, 40.5)
- removed the TP4 at (155.2, 40.5)
- removed the TP4 at (120.4, 76.5)
- removed the TP4 at (120.4, 58.5)
- removed the TP4 at (155.2, 112.5)
- removed the TP4 at (155.2, 58.5)
- removed the TP4 at (120.4, 112.5)
- removed the TP4 at (155.2, 76.5)
- removed the TP5 at (155.2, 43.1)
- removed the TP5 at (155.2, 61.1)
- removed the TP5 at (120.4, 115.1)
- removed the TP5 at (120.4, 97.1)
- removed the TP5 at (120.4, 61.1)
- removed the TP5 at (120.4, 79.1)
- removed the TP5 at (155.2, 79.1)
- removed the TP5 at (155.2, 115.1)
- removed the TP5 at (155.2, 97.1)
- removed the TP5 at (120.4, 43.1)
- removed the U1 at (113.5, 109.4)
- removed the U1 at (113.5, 37.4)
- removed the U1 at (148.2, 73.4)
- removed the U1 at (148.2, 91.4)
- removed the U1 at (113.5, 91.4)
- removed the U1 at (148.2, 109.4)
- removed the U1 at (113.5, 55.4)
- removed the U1 at (113.5, 73.4)
- removed the U1 at (148.2, 37.4)
- removed the U1 at (148.2, 55.4)
- removed the U2 at (118.9, 76.5)
- removed the U2 at (153.7, 58.5)
- removed the U2 at (153.7, 76.5)
- removed the U2 at (118.9, 94.5)
- removed the U2 at (118.9, 40.5)
- removed the U2 at (118.9, 58.5)
- removed the U2 at (153.7, 94.5)
- removed the U2 at (153.7, 40.5)
- removed the U2 at (153.7, 112.5)
- removed the U2 at (118.9, 112.5)
- added C2: 100nF, Capacitor_SMD:C_0402_1005Metric, F.Cu at (119.0, 31.6)
- added C3: CL05A475MP5NRNC, easyeda2kicad:C0402, F.Cu at (138.0, 28.8)
- added C4: CL05A475MP5NRNC, easyeda2kicad:C0402, F.Cu at (137.8, 31.2)
- added C5: CL05A475MP5NRNC, easyeda2kicad:C0402, F.Cu at (125.7, 34.3)
- added D1: HL-5050RGBW-S1-A27, easyeda2kicad:LED-SMD_8P-L5.0-W5.0-P1.20_HL-5050RGBW-S1-A27, F.Cu at (130.2, 28.4)
- added D2: HL-5050RGBW-S1-A27, easyeda2kicad:LED-SMD_8P-L5.0-W5.0-P1.20_HL-5050RGBW-S1-A27, F.Cu at (114.0, 27.2)
- added D3: 1N5819WS, easyeda2kicad:SOD-323_L1.8-W1.3-LS2.5-RD, F.Cu at (135.6, 25.8)
- added Q1: BSS138W_C28646265, easyeda2kicad:SOT-323-3_L2.1-W1.3-P1.30-LS2.3-BR, F.Cu at (136.2, 32.0)
- added Q2: BSS138W_C28646265, easyeda2kicad:SOT-323-3_L2.1-W1.3-P1.30-LS2.3-BR, F.Cu at (125.6, 32.2)
- added Q3: BSS138W_C28646265, easyeda2kicad:SOT-323-3_L2.1-W1.3-P1.30-LS2.3-BR, F.Cu at (125.6, 29.8)
- added Q4: BSS138W_C28646265, easyeda2kicad:SOT-323-3_L2.1-W1.3-P1.30-LS2.3-BR, F.Cu at (125.6, 27.4)
- added R1: 0402WGF1502TCE, easyeda2kicad:R0402, F.Cu at (118.0, 26.6)
- added R10: 4.7k, Resistor_SMD:R_0402_1005Metric, F.Cu at (134.0, 30.6)
- added R11: 4.7k, Resistor_SMD:R_0402_1005Metric, F.Cu at (135.6, 34.6)
- added R2: 0402WGF1502TCE, easyeda2kicad:R0402, F.Cu at (118.0, 27.8)
- added R3: 0402WGF1502TCE, easyeda2kicad:R0402, F.Cu at (118.0, 29.0)
- added R4: 0402WGF1502TCE, easyeda2kicad:R0402, F.Cu at (129.6, 24.4)
- added R5: 0402WGF1502TCE, easyeda2kicad:R0402, F.Cu at (130.8, 24.4)
- added R6: 0402WGF1502TCE, easyeda2kicad:R0402, F.Cu at (132.0, 24.4)
- added R7: 0402WGF4702TCE, easyeda2kicad:R0402, F.Cu at (118.0, 25.4)
- added R8: 0402WGF4702TCE, easyeda2kicad:R0402, F.Cu at (128.4, 24.4)
- added R9: 51k, Resistor_SMD:R_0402_1005Metric, F.Cu at (135.2, 24.4)
- added TP1: +, TestPoint:TestPoint_Pad_D4.0mm, B.Cu at (130.8, 29.8)
- added TP2: -, TestPoint:TestPoint_Pad_D4.0mm, B.Cu at (114.2, 29.4)
- added TP3: PA0, TestPoint:TestPoint_Pad_D1.5mm, B.Cu at (131.0, 36.4)
- added TP4: GND, TestPoint:TestPoint_Pad_D1.5mm, B.Cu at (133.2, 35.0)
- added TP5: V+, TestPoint:TestPoint_Pad_D1.5mm, B.Cu at (135.2, 33.4)
- added U1: ATtiny202-SSNR, Package_SO:SOIC-8_3.9x4.9mm_P1.27mm, F.Cu at (131.0, 34.2)
- added U2: IRM-H638T/TR2, OptoDevice:Everlight_IRM-H6xxT, F.Cu at (114.2, 33.4)
- added U3: PAM2803AAF095, easyeda2kicad:SOT-23-6_L2.9-W1.6-P0.95-LS2.8-BR, F.Cu at (135.2, 28.2)
- added U4: MBKK1608T1R5M, easyeda2kicad:L0603, F.Cu at (133.6, 23.8)
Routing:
- net VBATT: track 452.0 -> 30.0 mm, vias 140 -> 4
- net /PA2: track 425.1 -> 11.8 mm, vias 30 -> 0
- net /PA6: track 330.5 -> 9.37 mm, vias 20 -> 0
- net /PA7: track 323.9 -> 13.2 mm, vias 20 -> 0
- net /PA1: track 292.9 -> 4.67 mm, vias 10 -> 0
- net GND: track 286.3 -> 8.97 mm, vias 50 -> 16
- net /PA0: track 111.3 -> 5.80 mm, vias 10 -> 1
- net /PA3: track 58.1 -> 0.00 mm
- net /VREG: track 0.00 -> 33.1 mm
- net Net-(D1-Pad6): track 29.6 -> 1.28 mm
- net /red: track 0.00 -> 21.4 mm, vias 0 -> 2
- net Net-(D1-Pad8): track 18.8 -> 1.28 mm
- net Net-(D2-Pad8): track 14.1 -> 1.31 mm
- net Net-(D2-Pad6): track 14.1 -> 1.31 mm
- net Net-(D2-Pad4): track 14.0 -> 1.31 mm
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- added copper zone on B.Cu, net GND
- added copper zone on F.Cu, net GND
- removed copper zone on B.Cu, net VBATT
- removed copper zone on F.Cu, net VBATT
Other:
- board size 79.8 x 90.1 mm -> 32.8 x 16.2 mm
- board text added: "Alvarez"
- board text added: "BAT+"
- board text added: "BAT-"
- board text removed: "+"
- board text removed: "-"
- board text removed: "1"
- board text removed: "3"
- board text removed: "4"
- board text removed: "5"
- board text removed: "Brian Alvarez"
- board text removed: "CNC"
- board text removed: "PA0"
- board text removed: "v1.0"
